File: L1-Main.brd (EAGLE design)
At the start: 29 parts

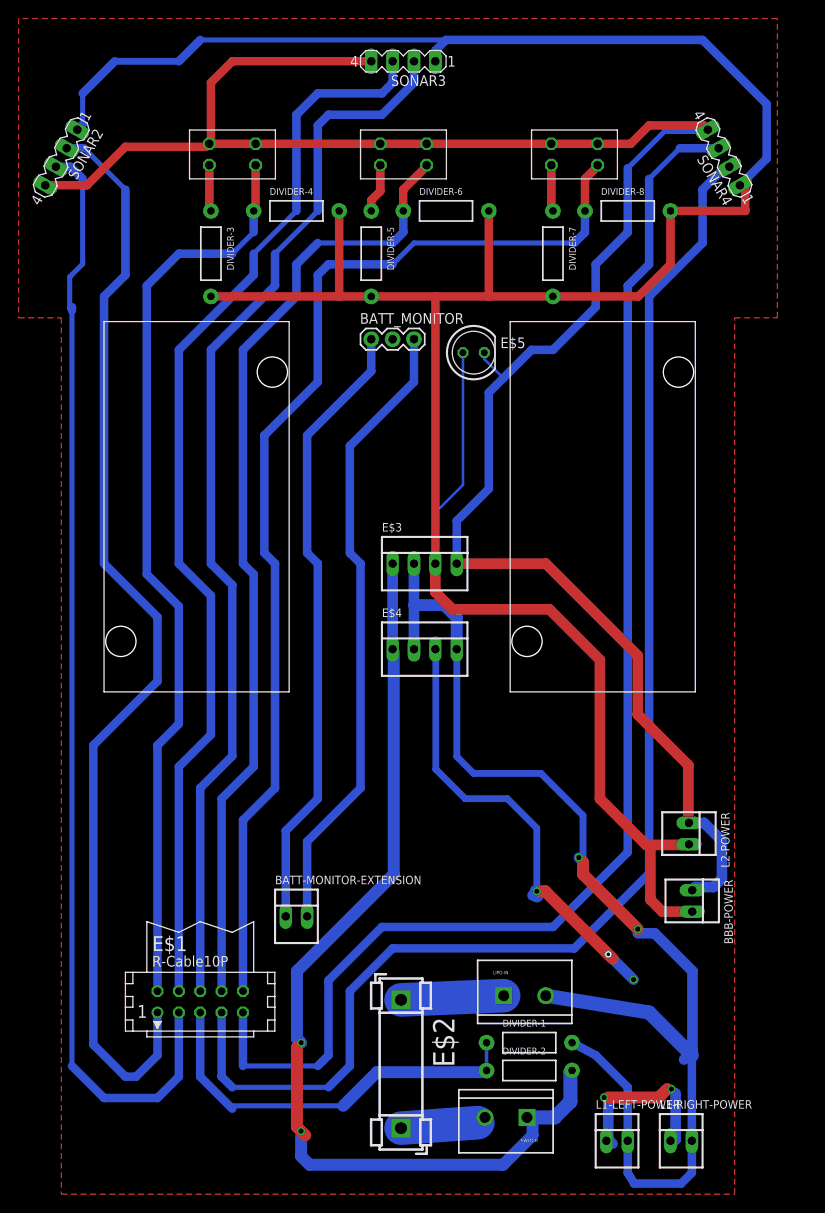
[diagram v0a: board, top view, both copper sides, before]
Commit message: redesigned all boards.
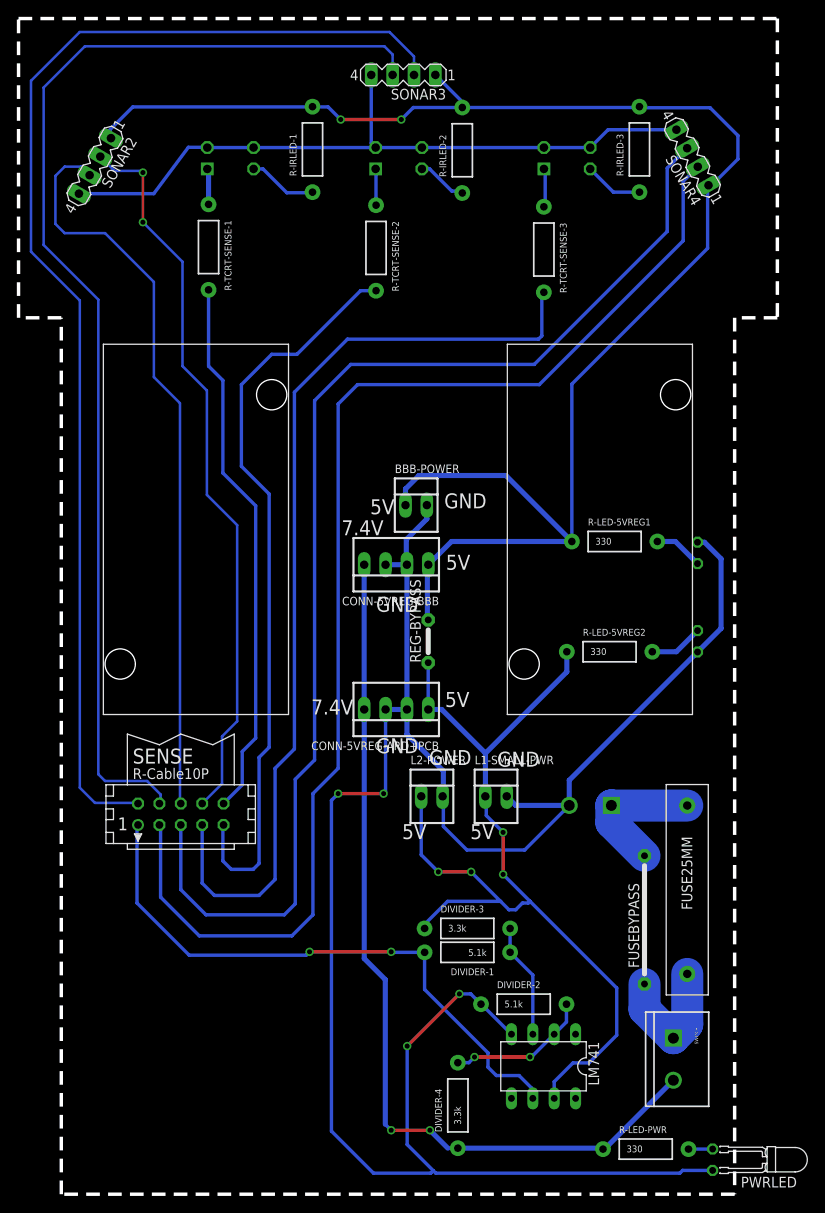
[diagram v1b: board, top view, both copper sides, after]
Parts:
- removed BATT-MONITOR-EXTENSION, L1-LEFT-POWER, L1-RIGHT-POWER: (no value), con-molex:22-23-2021
- removed BATT_MONITOR: (no value), SparkFun-Connectors:1X03
- removed DIVIDER-5, DIVIDER-6, DIVIDER-7, DIVIDER-8: (no value), SparkFun-Passives:AXIAL-0.4
- removed E$1: (no value), con-harting:CON10
- removed E$2: (no value), fuse:FUSE_HOLDER_5X20MM
- removed E$3, E$4: (no value), con-molex:22-23-2041
- removed E$5: (no value), led:LED5MM
- removed REG_BBB, REG_EXT: (no value), 5V3ARegulator:5V3A_REG
- added 5VREG-BBB, REG_ARD+PCB: (no value), 5V3ARegulator:5V3A_REG
- added CONN-5VREG-ARD+PCB, CONN-5VREG-BBB: (no value), con-molex:22-23-2041
- added FUSEBYPASS: (no value), jumper:15
- added L1-SMALL-PWR: 5V, con-molex:22-23-2021
- added LM741: (no value), 40xx:DIL08
- added PWR-SW: (no value), fuse25mm:FUSE25MM
- added PWRLED: green, led:LED3MM_H7,5MM
- added PWRLED1, PWRLED2: yellow, led:LED3MM_H7,5MM
- added R-IRLED-1, R-IRLED-2, R-IRLED-3, R-TCRT-SENSE-1, R-TCRT-SENSE-2, R-TCRT-SENSE-3: (no value), SparkFun-Passives:AXIAL-0.4
- added R-LED-5VREG1, R-LED-5VREG2, R-LED-PWR: 330, SparkFun-Passives:AXIAL-0.4
- added REG-BYPASS: (no value), jumper:05
- added SENSE: (no value), con-harting:CON10
- DIVIDER-1, DIVIDER-2: value (none) -> 5.1k
- DIVIDER-3, DIVIDER-4: value (none) -> 3.3k
- moved DIVIDER-4 108.0 mm to (47.1, 10.6), turned to 90 degrees
- moved DIVIDER-3 85.8 mm to (48.2, 31.6), turned to 0 degrees
- moved BBB-POWER 57.3 mm to (42.2, 81.9), turned to 0 degrees
- moved L2-POWER 30.9 mm to (44.0, 47.3), turned to 0 degrees
- moved LIPO-IN 26.0 mm to (65.4, 46.2), flipped to the bottom
- moved SWITCH 19.8 mm to (72.7, 18.5), turned to 270 degrees
- moved DIVIDER-1 13.0 mm to (48.2, 28.7), turned to 180 degrees
- moved DIVIDER-2 7.91 mm to (55.0, 22.6)
- moved TCRT3 5.42 mm to (55.0, 126.0), flipped to the bottom, turned to 180 degrees
- moved TCRT2 5.38 mm to (35.0, 126.0), flipped to the bottom, turned to 180 degrees
- moved TCRT1 5.36 mm to (15.0, 126.0), flipped to the bottom, turned to 180 degrees
- moved SONAR2 4.12 mm to (4.00, 122.2)
- moved SONAR4 3.74 mm to (75.0, 123.2)
- moved SONAR3 1.62 mm to (40.6, 133.0)
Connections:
- removed net S$3: E$2.2, SWITCH.2
- removed net S$41: DIVIDER-1.P$1, DIVIDER-2.P$1
- new net S$1: FUSEBYPASS.2, LIPO-IN.1, PWR-SW.PIN2
- new net S$26: R-TCRT-SENSE-3.P$2, SENSE.7
- new net S$27: R-TCRT-SENSE-2.P$2, SENSE.9
- new net S$28: R-TCRT-SENSE-1.P$2, SENSE.10
- new net S$29: BBB-POWER.1, CONN-5VREG-BBB.1, R-IRLED-1.P$2, R-IRLED-2.P$2, R-IRLED-3.P$2, R-LED-5VREG1.P$1, REG-BYPASS.2, SONAR2.1, SONAR3.1, SONAR4.1
- net S$10: now also SENSE.3, SONAR4.2; no longer DIVIDER-5.P$1, TCRT2.3
- net S$11: now also CONN-5VREG-ARD+PCB.1, DIVIDER-3.P$1, L1-SMALL-PWR.1, L2-POWER.1, LM741.7, R-LED-5VREG2.P$1, REG-BYPASS.1; no longer DIVIDER-7.P$1, TCRT3.3
- net S$12: now also SONAR2.4, SONAR3.4, SONAR4.4, TCRT1.EMITTER, TCRT1.LED-GND, TCRT2.EMITTER, TCRT2.LED-GND, TCRT3.EMITTER, TCRT3.LED-GND; no longer BATT-MONITOR-EXTENSION.1, BATT_MONITOR.1
- net S$13: now also R-TCRT-SENSE-2.P$1, TCRT2.COLLECTOR; no longer DIVIDER-4.P$1, E$1.2, TCRT1.4
- net S$14: now also DIVIDER-1.P$1, DIVIDER-3.P$2, LM741.3; no longer DIVIDER-6.P$1, E$1.8, TCRT2.4
- net S$15: now also DIVIDER-2.P$2, DIVIDER-4.P$2, LM741.2; no longer DIVIDER-8.P$1, E$1.10, TCRT3.4
- net S$16: now also DIVIDER-1.P$2, LM741.6, SENSE.1; no longer BBB-POWER.2, DIVIDER-3.P$2, DIVIDER-4.P$2, DIVIDER-5.P$2, DIVIDER-6.P$2, DIVIDER-7.P$2, DIVIDER-8.P$2, E$3.3, E$5.A, L2-POWER.2, SONAR2.1, SONAR3.1, SONAR4.1
- net S$17: now also BBB-POWER.2, CONN-5VREG-ARD+PCB.2, CONN-5VREG-ARD+PCB.3, CONN-5VREG-BBB.2, CONN-5VREG-BBB.3, DIVIDER-2.P$1, L1-SMALL-PWR.2, L2-POWER.2, LIPO-IN.2, LM741.4, PWRLED.K, PWRLED1.K, PWRLED2.A; no longer BATT-MONITOR-EXTENSION.2, BATT_MONITOR.3
- net S$18: now also R-IRLED-2.P$1, TCRT2.LED-VCC; no longer E$1.5
- net S$19: now also R-TCRT-SENSE-3.P$1, TCRT3.COLLECTOR; no longer E$1.6, SONAR3.2
- net S$2: now also FUSEBYPASS.1, PWR-SW.PIN1, SWITCH.1; no longer E$2.1, LIPO-IN.1
- net S$20: now also R-IRLED-3.P$1, TCRT3.LED-VCC; no longer E$1.7, SONAR4.2
- net S$21: now also SENSE.5, SONAR4.3; no longer E$1.4, SONAR3.3
- net S$22: now also SENSE.6, SONAR2.3; no longer E$1.9, SONAR4.3
- net S$23: now also SENSE.8, SONAR2.2; no longer SONAR2.4
- net S$24: now also SENSE.4, SONAR3.3; no longer E$3.1, E$4.1
- net S$25: now also SENSE.2, SONAR3.2; no longer E$3.2, E$4.2, E$4.4
- net S$4: now also PWRLED.A, R-LED-PWR.P$2; no longer DIVIDER-2.P$2, SWITCH.1
- net S$5: now also R-IRLED-1.P$1, TCRT1.LED-VCC; no longer E$1.3, SONAR2.3
- net S$6: now also CONN-5VREG-ARD+PCB.4, CONN-5VREG-BBB.4, DIVIDER-4.P$1, R-LED-PWR.P$1, SWITCH.2; no longer DIVIDER-1.P$2, L1-LEFT-POWER.2, L1-RIGHT-POWER.2, LIPO-IN.2
- net S$7: now also R-TCRT-SENSE-1.P$1, TCRT1.COLLECTOR; no longer E$1.1, SONAR2.2
- net S$8: now also PWRLED1.A, R-LED-5VREG1.P$2; no longer BBB-POWER.1, E$3.4, E$5.K, L2-POWER.1, SONAR3.4, SONAR4.4, TCRT1.1, TCRT1.2, TCRT2.1, TCRT2.2, TCRT3.1, TCRT3.2
- net S$9: now also PWRLED2.K, R-LED-5VREG2.P$2; no longer DIVIDER-3.P$1, TCRT1.3
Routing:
- net S$16: track 327.0 -> 70.5 mm, vias 0 -> 2
- net S$8: track 222.4 -> 5.86 mm
- net S$29: track 0.71 -> 191.8 mm, vias 0 -> 2
- net S$17: track 74.9 -> 249.5 mm, vias 0 -> 4
- net S$20: track 162.9 -> 6.99 mm
- net S$10: track 5.89 -> 150.2 mm
- net S$24: track 10.2 -> 140.2 mm
- net S$7: track 132.8 -> 4.27 mm
- net S$25: track 19.6 -> 145.4 mm
- net S$5: track 133.3 -> 10.2 mm
- net S$19: track 126.8 -> 4.63 mm
- net S$15: track 132.3 -> 17.0 mm, vias 0 -> 2
- net S$26: track 0.00 -> 113.3 mm, vias 1 -> 0
- net S$11: track 5.52 -> 115.9 mm, vias 0 -> 4
- net S$13: track 109.9 -> 4.33 mm
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- removed copper zone on layer 1, net S$1
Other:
- board outline added: 90.2 x 139.7 mm
- board text added: "5V"
- board text added: "7.4V"
- board text added: "GND"
